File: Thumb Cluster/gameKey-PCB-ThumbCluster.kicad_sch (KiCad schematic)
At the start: 4 parts, among them J0 Conn_01x06, J1 Conn_01x05

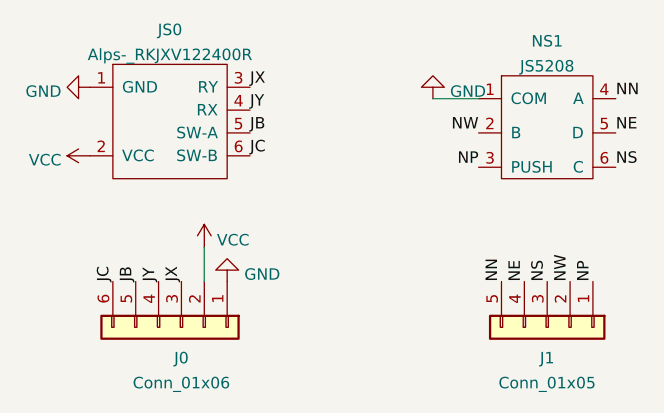
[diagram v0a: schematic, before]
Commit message: Critical - thumb nav switch was missing column pin Broke out away from common ground and improved labeling
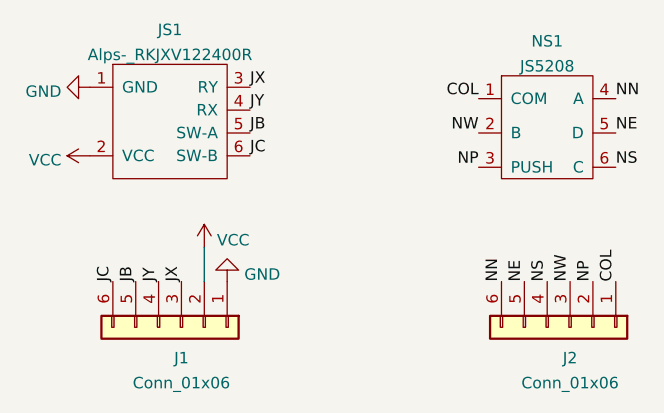
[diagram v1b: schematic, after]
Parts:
- removed J1: Conn_01x05, Connector_PinHeader_2.00mm:PinHeader_1x05_P2.00mm_Vertical_SMD_Pin1Left, symbol Connector_Generic:Conn_01x05
- added J2: Conn_01x06, Connector_PinHeader_2.00mm:PinHeader_1x06_P2.00mm_Vertical_SMD_Pin1Left, symbol Connector_Generic:Conn_01x06
- renumbered J0 to J1, JS0 to JS1
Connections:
- net GND: no longer NS1.1 (COM)
- net NE: now also J2.5 (Pin_5)
- net NN: now also J2.6 (Pin_6)
- net NP: now also J2.2 (Pin_2)
- net NS: now also J2.4 (Pin_4)
- net NW: now also J2.3 (Pin_3)
- new net COL: J2.1 (Pin_1), NS1.1 (COM)
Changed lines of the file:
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@@
 (kicad_sch (version 20211123) (generator eeschema)
   (paper "A4")
-  (wire (pts (xy 158.75 82.55) (xy 163.83 82.55))
-    (stroke (width 0) (type default) (color 0 0 0 0))
-  )
   (wire (pts (xy 133.35 99.06) (xy 133.35 102.87))
     (stroke (width 0) (type default) (color 0 0 0 0))
@@
     (effects (font (size 1.27 1.27)) (justify left bottom))
   )
+  (label "COL" (at 163.83 82.55 180)
+    (effects (font (size 1.27 1.27)) (justify right bottom))
+  )
   (label "JB" (at 138.43 86.36 0)
     (effects (font (size 1.27 1.27)) (justify left bottom))
@@
   )
   (label "JX" (at 130.81 102.87 90)
+    (effects (font (size 1.27 1.27)) (justify left bottom))
+  )
+  (label "COL" (at 179.07 102.87 90)
     (effects (font (size 1.27 1.27)) (justify left bottom))
   )
@@
   (symbol (lib_id "power:GND") (at 120.65 81.28 270) (unit 1)
     (in_bom yes) (on_board yes) (fields_autoplaced)
-    (property "Reference" "#PWR0105" (id 0) (at 114.3 81.28 0)
+    (property "Reference" "#PWR01" (id 0) (at 114.3 81.28 0)
       (effects (font (size 1.27 1.27)) hide)
     )
@@
     (pin "1")
   )
+  (symbol (lib_id "Connector_Generic:Conn_01x06") (at 173.99 107.95 270) (unit 1)
+    (in_bom yes) (on_board yes) (fields_autoplaced)
+    (property "Reference" "J2" (id 0) (at 173.99 111.3695 90))
+    (property "Value" "Conn_01x06" (id 1) (at 173.99 114.1446 90))
+    (property "Footprint" "Connector_PinHeader_2.00mm:PinHeader_1x06_P2.00mm_Vertical_SMD_Pin1Left" (id 2) (at 173.99 107.95 0)
+      (effects (font (size 1.27 1.27)) hide)
+    )
+    (property "Datasheet" "~" (id 3) (at 173.99 107.95 0)
+      (effects (font (size 1.27 1.27)) hide)
+    )
+    (pin "1")
+    (pin "2")
+    (pin "3")
+    (pin "4")
+    (pin "5")
+    (pin "6")
+  )
   (symbol (lib_id "power:GND") (at 135.89 102.87 180) (unit 1)
     (in_bom yes) (on_board yes) (fields_autoplaced)
-    (property "Reference" "#PWR0101" (id 0) (at 135.89 96.52 0)
+    (property "Reference" "#PWR04" (id 0) (at 135.89 96.52 0)
       (effects (font (size 1.27 1.27)) hide)
     )
@@
   (symbol (lib_id "Connector_Generic:Conn_01x06") (at 130.81 107.95 270) (unit 1)
     (in_bom yes) (on_board yes) (fields_autoplaced)
-    (property "Reference" "J0" (id 0) (at 130.81 111.3695 90))
+    (property "Reference" "J1" (id 0) (at 130.81 111.3695 90))
     (property "Value" "Conn_01x06" (id 1) (at 130.81 114.1446 90))
     (property "Footprint" "Connector_PinHeader_2.00mm:PinHeader_1x06_P2.00mm_Vertical_SMD_Pin1Left" (id 2) (at 130.81 107.95 0)
@@
   (symbol (lib_id "power:VCC") (at 120.65 88.9 90) (unit 1)
     (in_bom yes) (on_board yes) (fields_autoplaced)
-    (property "Reference" "#PWR0106" (id 0) (at 124.46 88.9 0)
+    (property "Reference" "#PWR02" (id 0) (at 124.46 88.9 0)
       (effects (font (size 1.27 1.27)) hide)
     )
@@
     )
     (pin "1")
-  )
-  (symbol (lib_id "Connector_Generic:Conn_01x05") (at 171.45 107.95 270) (unit 1)
-    (in_bom yes) (on_board yes) (fields_autoplaced)
-    (property "Reference" "J1" (id 0) (at 171.45 111.3695 90))
-    (property "Value" "Conn_01x05" (id 1) (at 171.45 114.1446 90))
-    (property "Footprint" "Connector_PinHeader_2.00mm:PinHeader_1x05_P2.00mm_Vertical_SMD_Pin1Left" (id 2) (at 171.45 107.95 0)
-      (effects (font (size 1.27 1.27)) hide)
-    )
-    (property "Datasheet" "~" (id 3) (at 171.45 107.95 0)
-      (effects (font (size 1.27 1.27)) hide)
-    )
-    (pin "1")
-    (pin "2")
-    (pin "3")
-    (pin "4")
-    (pin "5")
   )
   (symbol (lib_id "AndrewLib-Modules:JS5208") (at 171.45 86.36 0) (unit 1)
@@
   (symbol (lib_id "power:VCC") (at 133.35 99.06 0) (unit 1)
     (in_bom yes) (on_board yes) (fields_autoplaced)
-    (property "Reference" "#PWR0102" (id 0) (at 133.35 102.87 0)
+    (property "Reference" "#PWR03" (id 0) (at 133.35 102.87 0)
       (effects (font (size 1.27 1.27)) hide)
     )
@@
     (pin "1")
   )
-  (symbol (lib_id "power:GND") (at 158.75 82.55 180) (unit 1)
-    (in_bom yes) (on_board yes) (fields_autoplaced)
-    (property "Reference" "#PWR0103" (id 0) (at 158.75 76.2 0)
-      (effects (font (size 1.27 1.27)) hide)
-    )
-    (property "Value" "GND" (id 1) (at 160.655 81.759 0)
-      (effects (font (size 1.27 1.27)) (justify right))
-    )
-    (property "Footprint" "" (id 2) (at 158.75 82.55 0)
-      (effects (font (size 1.27 1.27)) hide)
-    )
-    (property "Datasheet" "" (id 3) (at 158.75 82.55 0)
-      (effects (font (size 1.27 1.27)) hide)
-    )
-    (pin "1")
-  )
   (symbol (lib_id "AndrewLib-Modules:Alps-_RKJXV122400R") (at 129.54 85.09 0) (unit 1)
     (in_bom yes) (on_board yes) (fields_autoplaced)
-    (property "Reference" "JS0" (id 0) (at 129.54 74.9005 0))
+    (property "Reference" "JS1" (id 0) (at 129.54 74.9005 0))
     (property "Value" "Alps-_RKJXV122400R" (id 1) (at 129.54 77.6756 0))
     (property "Footprint" "AndrewLib-Modules:Alps-RKJXV1224" (id 2) (at 129.54 74.93 0)
@@
   )
   (symbol_instances
+    (path "/6e69e5c9-097d-4c66-9fbb-33c4cc2a46b9"
+      (reference "#PWR01") (unit 1) (value "GND") (footprint "")
+    )
+    (path "/bd7d3c6e-6350-47ff-aa84-1eb0bbb4200f"
+      (reference "#PWR02") (unit 1) (value "VCC") (footprint "")
+    )
+    (path "/cbbf70ed-7bff-47f1-96e0-d27c8f090127"
+      (reference "#PWR03") (unit 1) (value "VCC") (footprint "")
+    )
     (path "/b535ebd0-a5f0-4816-9874-b0f294be53f5"
-      (reference "#PWR0101") (unit 1) (value "GND") (footprint "")
-    )
-    (path "/cbbf70ed-7bff-47f1-96e0-d27c8f090127"
-      (reference "#PWR0102") (unit 1) (value "VCC") (footprint "")
-    )
-    (path "/d3ffbaf8-6b20-4c43-96f7-9b88cf0a305f"
-      (reference "#PWR0103") (unit 1) (value "GND") (footprint "")
-    )
-    (path "/6e69e5c9-097d-4c66-9fbb-33c4cc2a46b9"
-      (reference "#PWR0105") (unit 1) (value "GND") (footprint "")
-    )
-    (path "/bd7d3c6e-6350-47ff-aa84-1eb0bbb4200f"
-      (reference "#PWR0106") (unit 1) (value "VCC") (footprint "")
+      (reference "#PWR04") (unit 1) (value "GND") (footprint "")
     )
     (path "/b948b3fe-622e-48cf-807a-d4974712723d"
-      (reference "J0") (unit 1) (value "Conn_01x06") (footprint "Connector_PinHeader_2.00mm:PinHeader_1x06_P2.00mm_Vertical_SMD_Pin1Left")
-    )
-    (path "/c5619795-34f9-4788-82a1-70162b563aae"
-      (reference "J1") (unit 1) (value "Conn_01x05") (footprint "Connector_PinHeader_2.00mm:PinHeader_1x05_P2.00mm_Vertical_SMD_Pin1Left")
+      (reference "J1") (unit 1) (value "Conn_01x06") (footprint "Connector_PinHeader_2.00mm:PinHeader_1x06_P2.00mm_Vertical_SMD_Pin1Left")
+    )
+    (path "/b06da986-ed15-478f-94e2-a7f44b1e6fbc"
+      (reference "J2") (unit 1) (value "Conn_01x06") (footprint "Connector_PinHeader_2.00mm:PinHeader_1x06_P2.00mm_Vertical_SMD_Pin1Left")
     )
     (path "/fb0bf2a0-d317-42f7-b022-b5e05481f6be"
-      (reference "JS0") (unit 1) (value "Alps-_RKJXV122400R") (footprint "AndrewLib-Modules:Alps-RKJXV1224")
+      (reference "JS1") (unit 1) (value "Alps-_RKJXV122400R") (footprint "AndrewLib-Modules:Alps-RKJXV1224")
     )
     (path "/c7af8405-da2e-4a34-b9b8-518f342f8995"
